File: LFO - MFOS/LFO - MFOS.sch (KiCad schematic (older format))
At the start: 97 parts, among them J1 CV1, J2 CV2, J3 CV3, J4 SIN, J5 RAMP, J6 SAW, J7 CV_PW, J8 SIN, J9 SQR, Q1 Q_NJFET_GSD, Q2 Q_NJFET_GSD, Q3 2N3904, Q4 2N3904, Q5 2N3906, Q6 2N3904, U1 LM13700, U2 TL082, U3 TL082, U4 LF442, U5 TL082, U6 TL082

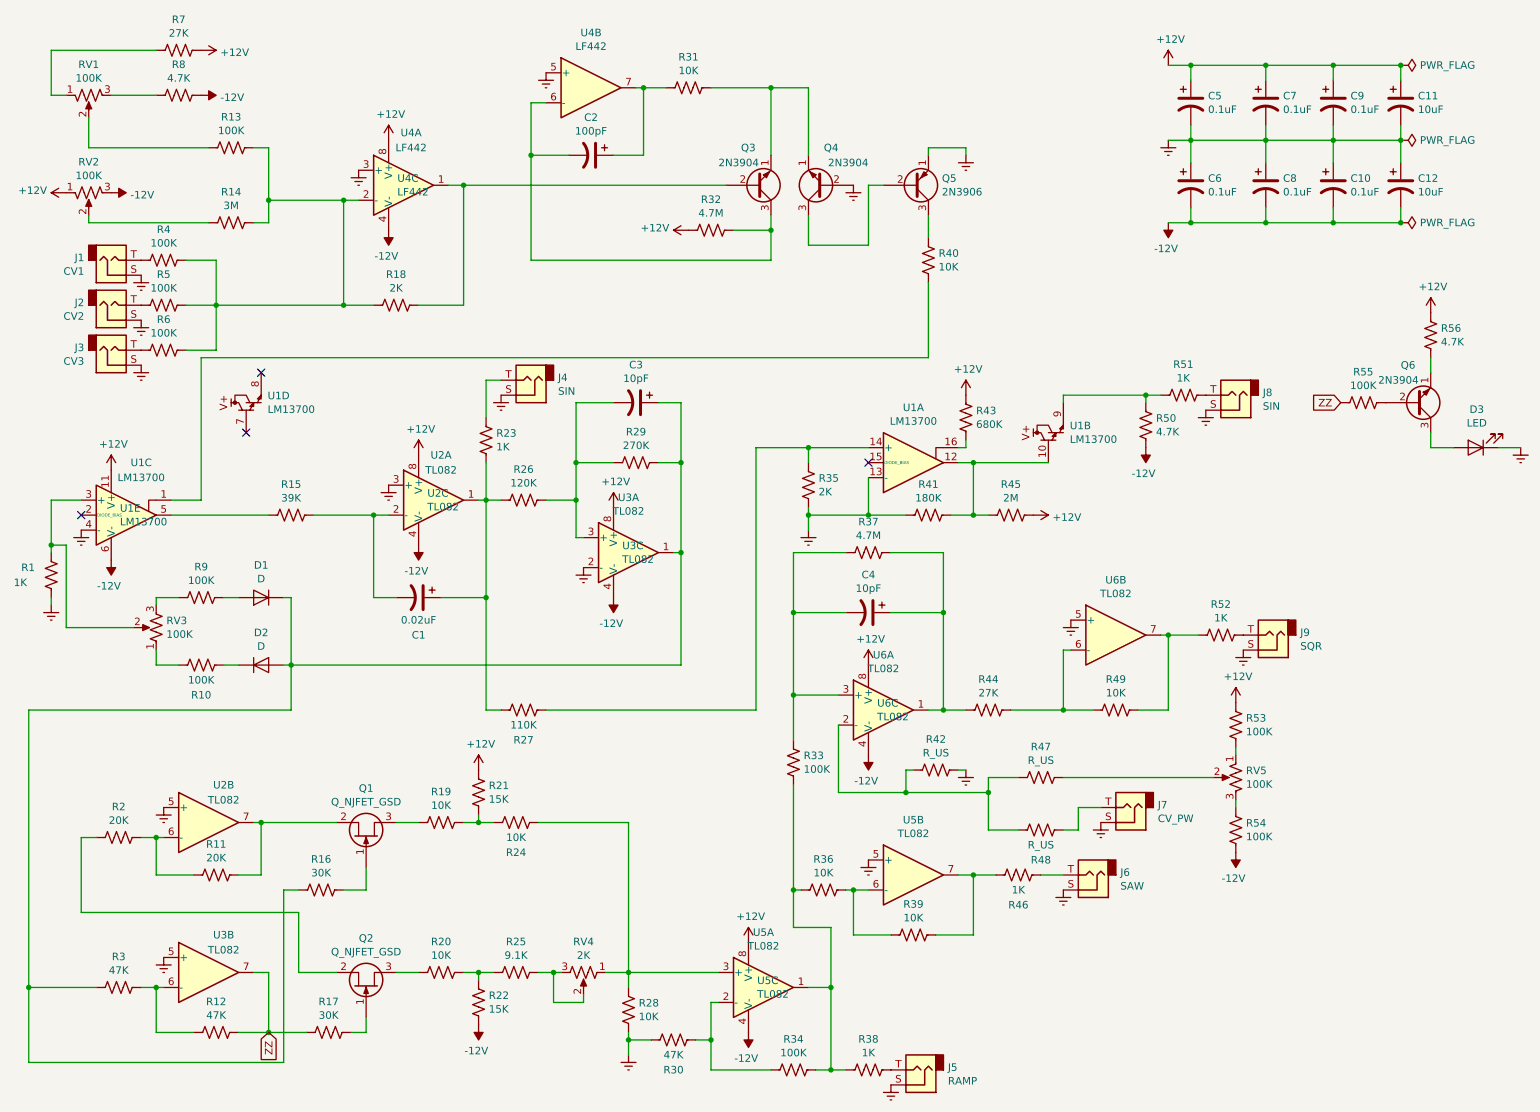
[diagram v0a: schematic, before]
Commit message: checked schematic and assigned footprints
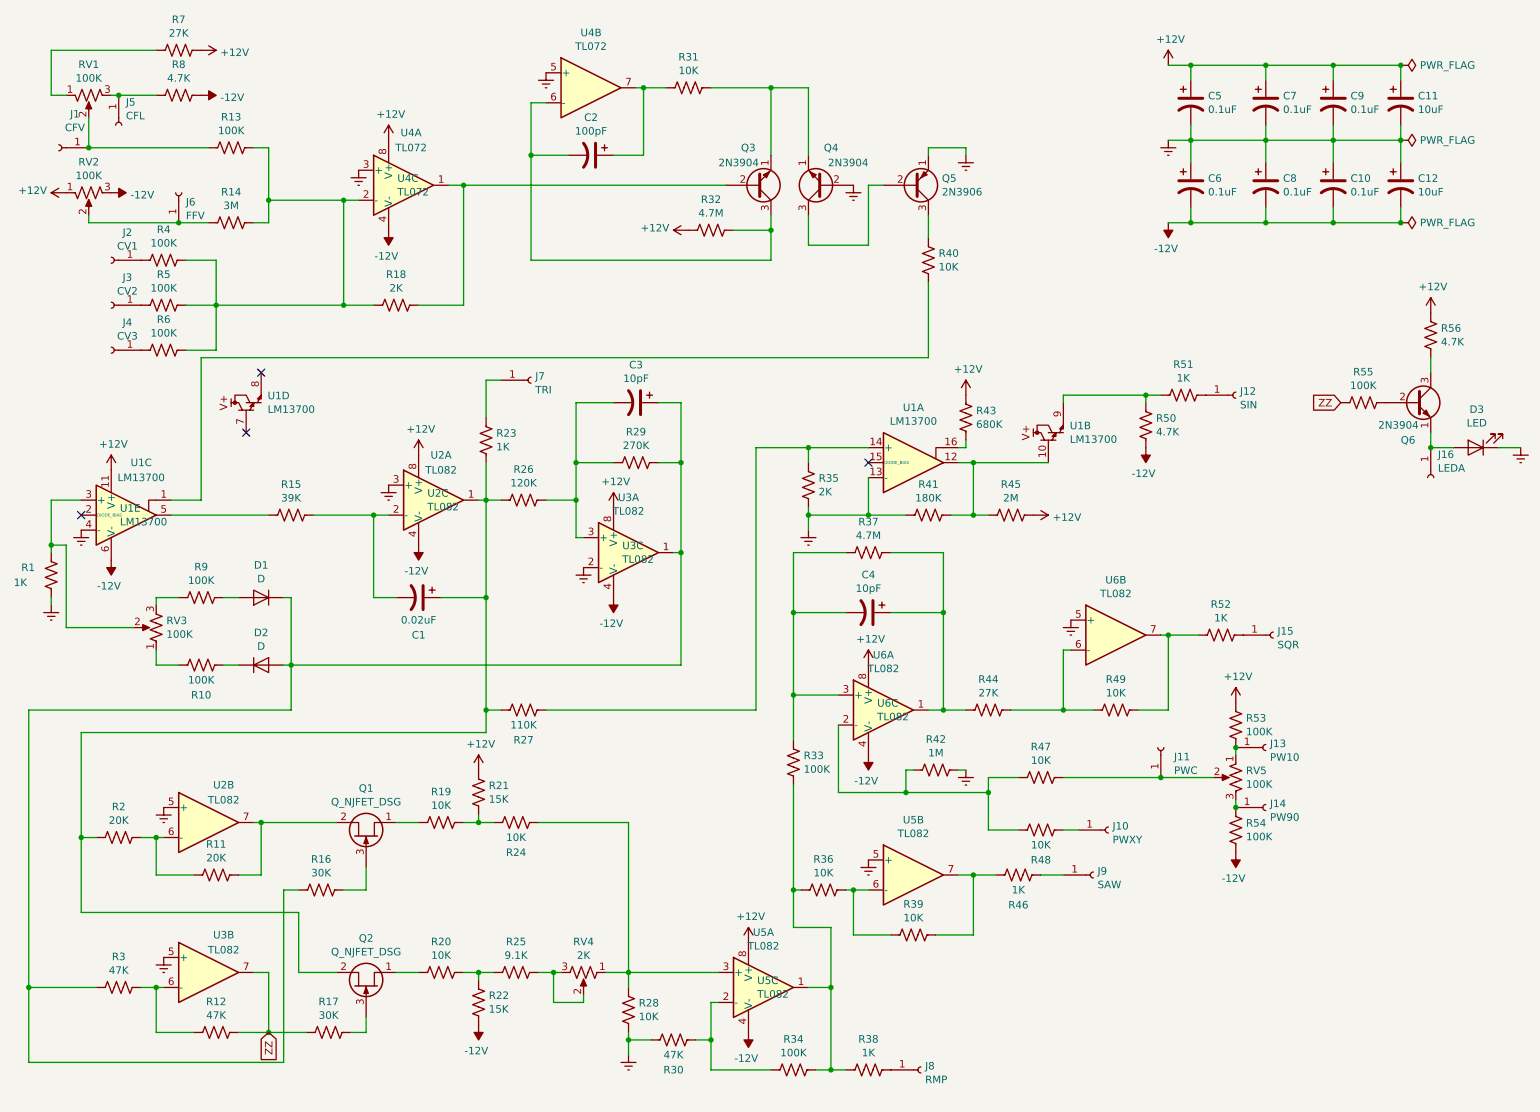
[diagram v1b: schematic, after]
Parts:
- removed J1: CV1, symbol Connector:AudioJack2
- removed J2: CV2, symbol Connector:AudioJack2
- removed J3: CV3, symbol Connector:AudioJack2
- removed J4, J8: SIN, symbol Connector:AudioJack2
- removed J5: RAMP, symbol Connector:AudioJack2
- removed J6: SAW, symbol Connector:AudioJack2
- removed J7: CV_PW, symbol Connector:AudioJack2
- removed J9: SQR, symbol Connector:AudioJack2
- removed Q1, Q2: Q_NJFET_GSD, symbol Device:Q_NJFET_GSD
- added J1: CFV, Connector_Wire:SolderWirePad_1x01_Drill1mm, symbol Connector:Conn_01x01_Female
- added J10: PWXY, Connector_Wire:SolderWirePad_1x01_Drill1mm, symbol Connector:Conn_01x01_Female
- added J11: PWC, Connector_Wire:SolderWirePad_1x01_Drill1mm, symbol Connector:Conn_01x01_Female
- added J12: SIN, Connector_Wire:SolderWirePad_1x01_Drill1mm, symbol Connector:Conn_01x01_Female
- added J13: PW10, Connector_Wire:SolderWirePad_1x01_Drill1mm, symbol Connector:Conn_01x01_Female
- added J14: PW90, Connector_Wire:SolderWirePad_1x01_Drill1mm, symbol Connector:Conn_01x01_Female
- added J15: SQR, Connector_Wire:SolderWirePad_1x01_Drill1mm, symbol Connector:Conn_01x01_Female
- added J16: LEDA, Connector_Wire:SolderWirePad_1x01_Drill1mm, symbol Connector:Conn_01x01_Female
- added J2: CV1, Connector_Wire:SolderWirePad_1x01_Drill1mm, symbol Connector:Conn_01x01_Female
- added J3: CV2, Connector_Wire:SolderWirePad_1x01_Drill1mm, symbol Connector:Conn_01x01_Female
- added J4: CV3, Connector_Wire:SolderWirePad_1x01_Drill1mm, symbol Connector:Conn_01x01_Female
- added J5: CFL, Connector_Wire:SolderWirePad_1x01_Drill1mm, symbol Connector:Conn_01x01_Female
- added J6: FFV, Connector_Wire:SolderWirePad_1x01_Drill1mm, symbol Connector:Conn_01x01_Female
- added J7: TRI, Connector_Wire:SolderWirePad_1x01_Drill1mm, symbol Connector:Conn_01x01_Female
- added J8: RMP, Connector_Wire:SolderWirePad_1x01_Drill1mm, symbol Connector:Conn_01x01_Female
- added J9: SAW, Connector_Wire:SolderWirePad_1x01_Drill1mm, symbol Connector:Conn_01x01_Female
- added Q1, Q2: Q_NJFET_DSG, Package_TO_SOT_THT:TO-92_Inline_Wide, symbol Device:Q_NJFET_DSG
- C1, C2, C3, C4: footprint (none) -> Capacitor_THT:C_Rect_L7.0mm_W2.5mm_P5.00mm
- C10, C11, C12, C5, C6, C7, C8, C9: footprint (none) -> Capacitor_THT:CP_Radial_D4.0mm_P2.00mm
- D1, D2: footprint (none) -> Diode_THT:D_T-1_P5.08mm_Horizontal
- Q3, Q4, Q5, Q6: footprint Package_TO_SOT_THT:TO-92_Inline -> Package_TO_SOT_THT:TO-92_Inline_Wide
- R1, R10, R11, R12, R13, R14, R15, R16, R17, R18, R19, R2, R20, R21, R22, R23, R24, R25, R26, R27, R28, R29, R3, R30, R31, R32, R33, R34, R35, R36, R37, R38, R39, R4, R40, R41, R43, R44, R45, R46, R49, R5, R50, R51, R52, R53, R54, R55, R56, R6, R7, R8, R9: footprint (none) -> Resistor_THT:R_Axial_DIN0207_L6.3mm_D2.5mm_P7.62mm_Horizontal
- R42: value R_US -> 1M; footprint (none) -> Resistor_THT:R_Axial_DIN0207_L6.3mm_D2.5mm_P7.62mm_Horizontal
- R47, R48: value R_US -> 10K; footprint (none) -> Resistor_THT:R_Axial_DIN0207_L6.3mm_D2.5mm_P7.62mm_Horizontal
- RV3, RV4: footprint (none) -> Potentiometer_THT:Potentiometer_Runtron_RM-065_Vertical
- U1: footprint (none) -> Package_DIP:DIP-16_W7.62mm_Socket
- U2, U3, U5, U6: footprint (none) -> Package_DIP:DIP-8_W7.62mm_Socket
- U4: value LF442 -> TL072; footprint (none) -> Package_DIP:DIP-8_W7.62mm_Socket
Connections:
- net at R13.2, RV1.2: now also J1.1 (Pin_1)
- net at R8.2, RV1.3: now also J5.1 (Pin_1)
- net at R14.2, RV2.2: now also J6.1 (Pin_1)
- net at R4.2: now also J2.1 (Pin_1)
- net at R5.2: now also J3.1 (Pin_1)
- net at R6.2: now also J4.1 (Pin_1)
- net at C1.1, R23.1, R26.2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: now also R2.2, Q2.2 (S)
- net at Q6.1 (E): now also D3.2 (A), J16.1 (Pin_1); no longer R56.1
- net at Q6.3 (C): now also R56.1; no longer D3.2 (A)
- net at R51.1: now also J12.1 (Pin_1)
- net at R11.1, U2.7: now also Q1.2 (S)
- net at R16.1: now also Q1.3 (G)
- net at R17.1: now also Q2.3 (G)
- net at R20.2: now also Q2.1 (D)
- net at R19.2: now also Q1.1 (D)
- net at R38.1: now also J8.1 (Pin_1)
- net at R52.2: now also J15.1 (Pin_1)
- net at R53.2, RV5.1: now also J13.1 (Pin_1)
- net at R47.2, RV5.2: now also J11.1 (Pin_1)
- net at R48.2: now also J10.1 (Pin_1)
- net at R54.1, RV5.3: now also J14.1 (Pin_1)
- net at R23.2: now also J7.1 (Pin_1)
- net at R46.1: now also J9.1 (Pin_1)

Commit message: placed components in general location on pcb uwu
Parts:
- added J17: +12V_Conn, Connector_Wire:SolderWirePad_1x02_P3.81mm_Drill1mm, symbol Connector:Conn_01x02_Female
- added J18: GND_Conn, Connector_Wire:SolderWirePad_1x02_P3.81mm_Drill1mm, symbol Connector:Conn_01x02_Female
- added J19: -12V_Conn, Connector_Wire:SolderWirePad_1x02_P3.81mm_Drill1mm, symbol Connector:Conn_01x02_Female
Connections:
- net +12V: now also J17.1 (Pin_1), J17.2 (Pin_2)
- net -12V: now also J19.1 (Pin_1), J19.2 (Pin_2)
- net Earth: now also J18.1 (Pin_1), J18.2 (Pin_2)
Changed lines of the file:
@@
 $EndComp
 Connection ~ 9950 3400
+$Comp
+L Connector:Conn_01x02_Female J17
+U 1 1 60223451
+P 7850 650
+F 0 "J17" V 7788 462 50  0000 R CNN
+F 1 "+12V_Conn" V 7697 462 50  0000 R CNN
+F 2 "Connector_Wire:SolderWirePad_1x02_P3.81mm_Drill1mm" H 7850 650 50  0001 C CNN
+F 3 "~" H 7850 650 50  0001 C CNN
+	1    7850 650
+	0    -1   -1   0
+$EndComp
+$Comp
+L Connector:Conn_01x02_Female J18
+U 1 1 60224A8B
+P 7850 1150
+F 0 "J18" V 7788 962 50  0000 R CNN
+F 1 "GND_Conn" V 7697 962 50  0000 R CNN
+F 2 "Connector_Wire:SolderWirePad_1x02_P3.81mm_Drill1mm" H 7850 1150 50  0001 C CNN
+F 3 "~" H 7850 1150 50  0001 C CNN
+	1    7850 1150
+	0    -1   -1   0
+$EndComp
+$Comp
+L Connector:Conn_01x02_Female J19
+U 1 1 60225244
+P 7850 1700
+F 0 "J19" V 7788 1512 50  0000 R CNN
+F 1 "-12V_Conn" V 7697 1512 50  0000 R CNN
+F 2 "Connector_Wire:SolderWirePad_1x02_P3.81mm_Drill1mm" H 7850 1700 50  0001 C CNN
+F 3 "~" H 7850 1700 50  0001 C CNN
+	1    7850 1700
+	0    -1   -1   0
+$EndComp
+Wire Wire Line
+	8200 850  7950 850
+Connection ~ 8200 850
+Wire Wire Line
+	7850 850  7950 850
+Connection ~ 7950 850
+Wire Wire Line
+	7850 1350 7950 1350
+Wire Wire Line
+	8200 1350 7950 1350
+Connection ~ 8200 1350
+Connection ~ 7950 1350
+Wire Wire Line
+	7850 1900 7950 1900
+Wire Wire Line
+	7950 1900 8200 1900
+Connection ~ 7950 1900
+Connection ~ 8200 1900
 $EndSCHEMATC

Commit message: hi i miight have done smth i dont remember uwu
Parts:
- C10, C5, C6, C7, C8, C9: footprint Capacitor_THT:CP_Radial_D4.0mm_P2.00mm -> Capacitor_THT:C_Rect_L7.0mm_W2.5mm_P5.00mm
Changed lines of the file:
@@
 F 0 "C5" H 8465 1146 50  0000 L CNN
 F 1 "0.1uF" H 8465 1055 50  0000 L CNN
-F 2 "Capacitor_THT:CP_Radial_D4.0mm_P2.00mm" H 8350 1100 50  0001 C CNN
+F 2 "Capacitor_THT:C_Rect_L7.0mm_W2.5mm_P5.00mm" H 8350 1100 50  0001 C CNN
 F 3 "~" H 8350 1100 50  0001 C CNN
 	1    8350 1100
@@
 F 0 "C7" H 8965 1146 50  0000 L CNN
 F 1 "0.1uF" H 8965 1055 50  0000 L CNN
-F 2 "Capacitor_THT:CP_Radial_D4.0mm_P2.00mm" H 8850 1100 50  0001 C CNN
+F 2 "Capacitor_THT:C_Rect_L7.0mm_W2.5mm_P5.00mm" H 8850 1100 50  0001 C CNN
 F 3 "~" H 8850 1100 50  0001 C CNN
 	1    8850 1100
@@
 F 0 "C9" H 9415 1146 50  0000 L CNN
 F 1 "0.1uF" H 9415 1055 50  0000 L CNN
-F 2 "Capacitor_THT:CP_Radial_D4.0mm_P2.00mm" H 9300 1100 50  0001 C CNN
+F 2 "Capacitor_THT:C_Rect_L7.0mm_W2.5mm_P5.00mm" H 9300 1100 50  0001 C CNN
 F 3 "~" H 9300 1100 50  0001 C CNN
 	1    9300 1100
@@
 F 0 "C6" H 8465 1696 50  0000 L CNN
 F 1 "0.1uF" H 8465 1605 50  0000 L CNN
-F 2 "Capacitor_THT:CP_Radial_D4.0mm_P2.00mm" H 8350 1650 50  0001 C CNN
+F 2 "Capacitor_THT:C_Rect_L7.0mm_W2.5mm_P5.00mm" H 8350 1650 50  0001 C CNN
 F 3 "~" H 8350 1650 50  0001 C CNN
 	1    8350 1650
@@
 F 0 "C8" H 8965 1696 50  0000 L CNN
 F 1 "0.1uF" H 8965 1605 50  0000 L CNN
-F 2 "Capacitor_THT:CP_Radial_D4.0mm_P2.00mm" H 8850 1650 50  0001 C CNN
+F 2 "Capacitor_THT:C_Rect_L7.0mm_W2.5mm_P5.00mm" H 8850 1650 50  0001 C CNN
 F 3 "~" H 8850 1650 50  0001 C CNN
 	1    8850 1650
@@
 F 0 "C10" H 9415 1696 50  0000 L CNN
 F 1 "0.1uF" H 9415 1605 50  0000 L CNN
-F 2 "Capacitor_THT:CP_Radial_D4.0mm_P2.00mm" H 9300 1650 50  0001 C CNN
+F 2 "Capacitor_THT:C_Rect_L7.0mm_W2.5mm_P5.00mm" H 9300 1650 50  0001 C CNN
 F 3 "~" H 9300 1650 50  0001 C CNN
 	1    9300 1650
